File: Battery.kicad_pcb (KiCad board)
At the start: 2 copper layers, 95.9 x 90.2 mm, 10 parts, among them J1 PC104-8BIT, J2 PC104PTH, J3 PC104PTH, J4 PC104PTH, J5 PC104PTH

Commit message: balancing enabled by default using 1k PD. Can override by pulling line high from OBC
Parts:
- turned BT2 to 270 degrees
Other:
- board text removed: "GPS Coax slot location and dimentions are provisional. Consider structural integrity of the board with cables connected."
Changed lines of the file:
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@@
 (kicad_pcb (version 4) (host pcbnew 4.0.7-e2-6376~58~ubuntu16.04.1)
   (general
-    (links 0)
+    (links 1)
     (no_connects 1)
-    (area 104.924999 44.754999 200.965001 135.075001)
+    (area 20.5 22.899999 253.885715 168.15)
     (thickness 1.6)
-    (drawings 25)
+    (drawings 24)
     (tracks 0)
     (zones 0)
@@
   )
   (module SFUSat:1042-BattHolder (layer F.Cu)
-    (at 169 90 90)
-    (fp_text reference BT2 (at -40.2 7.6 360) (layer F.SilkS)
-      (effects (font (size 1 1) (thickness 0.15)))
-    )
-    (fp_text value Battery_Cell (at 11.8 -11.8 90) (layer F.Fab)
+    (at 169 90 270)
+    (fp_text reference BT2 (at -40.2 7.6 540) (layer F.SilkS)
+      (effects (font (size 1 1) (thickness 0.15)))
+    )
+    (fp_text value Battery_Cell (at 11.8 -11.8 270) (layer F.Fab)
       (effects (font (size 1 1) (thickness 0.15)))
     )
@@
     (fp_line (start -38.6 -10.4) (end 38.45 -10.4) (layer F.SilkS) (width 0.15))
     (fp_line (start -38.6 10.25) (end 38.45 10.25) (layer F.SilkS) (width 0.15))
-    (pad "" np_thru_hole circle (at 27.6 -8 90) (size 4.5 4.5) (drill 3.45) (layers *.Cu *.Mask))
-    (pad "" np_thru_hole circle (at -27.6 8 90) (size 4.5 4.5) (drill 3.45) (layers *.Cu *.Mask))
-    (pad "" np_thru_hole circle (at 35.82 8 90) (size 3.3 3.3) (drill 2.39) (layers *.Cu *.Mask))
-    (pad 2 smd rect (at 39.67 0 90) (size 7.46 6.47) (layers F.Cu F.Paste F.Mask)
+    (pad "" np_thru_hole circle (at 27.6 -8 270) (size 4.5 4.5) (drill 3.45) (layers *.Cu *.Mask))
+    (pad "" np_thru_hole circle (at -27.6 8 270) (size 4.5 4.5) (drill 3.45) (layers *.Cu *.Mask))
+    (pad "" np_thru_hole circle (at 35.82 8 270) (size 3.3 3.3) (drill 2.39) (layers *.Cu *.Mask))
+    (pad 2 smd rect (at 39.67 0 270) (size 7.46 6.47) (layers F.Cu F.Paste F.Mask)
       (net 70 GND))
-    (pad 1 smd rect (at -39.67 0 90) (size 7.46 6.47) (layers F.Cu F.Paste F.Mask)
+    (pad 1 smd rect (at -39.67 0 270) (size 7.46 6.47) (layers F.Cu F.Paste F.Mask)
       (net 68 "Net-(BT1-Pad2)"))
     (model ../../../../../home/tobi/Cubesat/Battery/KiCad-Lib/SFUSat.pretty/1042.wrl
@@
     (effects (font (size 3 3) (thickness 0.3)))
   )
-  (gr_text "GPS Coax slot location and dimentions are provisional.\nConsider structural integrity of the board with cables connected." (at 20.5 65.5) (layer Cmts.User)
-    (effects (font (size 1.5 1.5) (thickness 0.3)) (justify left))
-  )
   (gr_line (start 105 44.83) (end 200.885 44.83) (layer Edge.Cuts) (width 0.15))

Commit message: layout complete
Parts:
- added C1: 0.1uF, SFUSat-cap:C_0603, F.Cu at (118.0, 69.2)
- added C2: 0.1uF, SFUSat-cap:C_0603, F.Cu at (114.8, 69.2)
- added C3: 0.33uF, SFUSat-cap:C_0805, F.Cu at (113.5, 72.5)
- added C4: 0.1uF, SFUSat-cap:C_0603, F.Cu at (115.8, 75.8)
- added G***: LOGO, SFUSat:SFUSat_15mm_2, B.Cu at (120.0, 72.0)
- added J10: TEST_1P, SFUSat:Measurement_Point_Round-SMD-Pad_Big, F.Cu at (109.0, 89.0)
- added J11: B3B-XH-A(LF)(SN), SFUSat:B3B-XH-A, B.Cu at (116.0, 96.0)
- added J12: B3B-XH-A(LF)(SN), SFUSat:B3B-XH-A, F.Cu at (116.0, 116.0)
- added J6: B3B-XH-A(LF)(SN), SFUSat:B3B-XH-A, F.Cu at (116.0, 106.0)
- added J7: TEST_1P, SFUSat:Measurement_Point_Round-SMD-Pad_Big, F.Cu at (108.0, 79.0)
- added J8: TEST_1P, SFUSat:Measurement_Point_Round-SMD-Pad_Big, F.Cu at (108.0, 75.0)
- added J9: TEST_1P, SFUSat:Measurement_Point_Round-SMD-Pad_Big, F.Cu at (115.0, 89.0)
- added R1: DNP, SFUSat-res:R_0402, F.Cu at (117.2, 77.5)
- added R2: 1k, SFUSat-res:R_0402, F.Cu at (115.2, 77.5)
- added R3: 160R, SFUSat-res:R_0603, F.Cu at (119.2, 72.8)
- added R4: 250R, SFUSat-res:R_0603, F.Cu at (117.2, 66.0)
- added R5: 100R, SFUSat-res:R_0603, F.Cu at (115.5, 66.0)
- added R6: 100R, SFUSat-res:R_0603, F.Cu at (118.5, 75.8)
- added R7: DNP, SFUSat-res:R_0603, F.Cu at (109.0, 83.0)
- added U1: BQ29209, SFUSat:VDFN-8, F.Cu at (116.2, 72.5)
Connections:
- BT2 pad 2: GND -> /SeriesBatteryCell/PACK-
- J1 pad 12A: Net-(J1-Pad12A) -> /OVR_VLT
- J1 pad 13A: Net-(J1-Pad13A) -> /~CB_EN
- J1 pad 1B: Net-(J1-Pad1B) -> GND
- J1 pad 32A: Net-(J1-Pad32A) -> GND
- J1 pad 32B: Net-(J1-Pad32B) -> GND
- J2 pad 1: Net-(J2-Pad1) -> GND
- J3 pad 1: Net-(J3-Pad1) -> GND
- J4 pad 1: Net-(J4-Pad1) -> GND
- J5 pad 1: Net-(J5-Pad1) -> GND
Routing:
- net /SeriesBatteryCell/PACK-: track 0.00 -> 142.0 mm, vias 0 -> 10
- net /OVR_VLT: track 0.00 -> 98.5 mm, vias 0 -> 2
- net /~CB_EN: track 0.00 -> 98.2 mm, vias 0 -> 2
- net /SeriesBatteryCell/PACK+: track 0.00 -> 90.0 mm
- net Net-(BT1-Pad2): track 0.00 -> 66.1 mm
- net Net-(J11-Pad1): track 0.00 -> 20.0 mm
- net Net-(C1-Pad2): track 0.00 -> 6.04 mm
- net Net-(C1-Pad1): track 0.00 -> 4.84 mm
- net Net-(R5-Pad2): track 0.00 -> 4.45 mm, vias 0 -> 2
- net Net-(C4-Pad1): track 0.00 -> 3.06 mm
- net Net-(C3-Pad1): track 0.00 -> 1.97 mm
- net GND: track 0.00 -> 1.25 mm, vias 0 -> 1
- added copper zone on F.Cu, net /SeriesBatteryCell/PACK-
- added copper zone on B.Cu, net GND
- added copper zone on F.Cu, net GND
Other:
- board text added: "COM"
- board text added: "DEPLOYMENT"
- board text added: "EN"
- board text added: "NC"
- board text added: "OV"
- board text added: "SFU Satellite Design Team Battery Board Rev. 1"
- board text added: "over voltage"
- board text added: "pack+"
- board text added: "pack-"
- board text added: "return"

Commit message: moved bottom side DC connector to avoid the RFB pin path on the eps board
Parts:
- moved J11 7.21 mm to (112.0, 90.0)
- moved J10 4.21 mm to (110.3, 85.0)
- moved J9 4.12 mm to (116.0, 85.0)
- moved R7 1.02 mm to (108.8, 82.0)
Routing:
- net /SeriesBatteryCell/PACK+: track 90.0 -> 79.9 mm
- net Net-(J11-Pad1): track 20.0 -> 27.7 mm
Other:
- board text added: "+"
- board text added: "-"
- board text added: "1A"
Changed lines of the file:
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@@
     (links 43)
     (no_connects 0)
-    (area 104.924999 44.754999 200.965001 135.075001)
+    (area 83.114286 22.899999 253.885715 168.15)
     (thickness 1.6)
-    (drawings 40)
-    (tracks 134)
+    (drawings 45)
+    (tracks 136)
     (zones 0)
     (modules 30)
@@
   (module SFUSat:1042-BattHolder (layer F.Cu)
     (at 169 90 270)
-    (fp_text reference BT2 (at -40.2 7.6 540) (layer F.SilkS)
+    (fp_text reference BT2 (at -40.6 -5.6 540) (layer F.SilkS)
       (effects (font (size 1 1) (thickness 0.15)))
     )
@@
   )
   (module SFUSat:Measurement_Point_Round-SMD-Pad_Big (layer F.Cu)
-    (at 115 89)
+    (at 116 85)
     (descr "Mesurement Point, Round, SMD Pad, DM 3mm,")
     (tags "Mesurement Point Round SMD Pad 3mm")
@@
   )
   (module SFUSat:Measurement_Point_Round-SMD-Pad_Big (layer F.Cu)
-    (at 109 89)
+    (at 110.3 85)
     (descr "Mesurement Point, Round, SMD Pad, DM 3mm,")
     (tags "Mesurement Point Round SMD Pad 3mm")
@@
   )
   (module SFUSat:B3B-XH-A (layer B.Cu)
-    (at 116 96)
-    (fp_text reference J11 (at -6 1 90) (layer B.SilkS)
+    (at 112 90)
+    (fp_text reference J11 (at -0.1 4.8 180) (layer B.SilkS)
       (effects (font (size 1 1) (thickness 0.15)) (justify mirror))
     )
@@
   )
   (module SFUSat-res:R_0603 (layer F.Cu)
-    (at 109 83 180)
+    (at 108.8 82 180)
     (descr "Resistor SMD 0603, reflow soldering, Vishay (see dcrcw.pdf)")
     (tags "resistor 0603")
     (attr smd)
-    (fp_text reference R7 (at 0 -1.45 180) (layer F.SilkS)
+    (fp_text reference R7 (at 2.5 0.1 180) (layer F.SilkS)
       (effects (font (size 1 1) (thickness 0.15)))
     )
@@
       (xy -0.05114 -0.609094)) (layer B.SilkS) (width 0.01))
   )
+  (gr_text 1A (at 190.8 131.9) (layer F.SilkS)
+    (effects (font (size 1.5 1.5) (thickness 0.3)))
+  )
+  (gr_text - (at 162.9 130.4) (layer F.SilkS)
+    (effects (font (size 3 3) (thickness 0.3)))
+  )
+  (gr_text + (at 162.8 48) (layer F.SilkS)
+    (effects (font (size 3 3) (thickness 0.3)))
+  )
+  (gr_text - (at 130.9 48.5) (layer F.SilkS)
+    (effects (font (size 3 3) (thickness 0.3)))
+  )
+  (gr_text + (at 130.3 130.9) (layer F.SilkS)
+    (effects (font (size 3 3) (thickness 0.3)))
+  )
+  (gr_text "SFU Satellite Design Team\nBattery Board Rev. 1" (at 112 73 270) (layer B.SilkS)
+    (effects (font (size 1.5 1.5) (thickness 0.2)) (justify mirror))
+  )
   (gr_text OV (at 194 101) (layer F.SilkS)
     (effects (font (size 1 1) (thickness 0.15)))
   )
-  (gr_text EN (at 194 98 360) (layer F.SilkS)
+  (gr_text EN (at 194 98) (layer F.SilkS)
     (effects (font (size 1 1) (thickness 0.15)))
-  )
-  (gr_text "SFU Satellite Design Team\nBattery Board Rev. 1" (at 112 73 270) (layer B.SilkS)
-    (effects (font (size 1.5 1.5) (thickness 0.2)) (justify mirror))
   )
   (gr_text DEPLOYMENT (at 108 116 270) (layer F.SilkS)
@@
     (effects (font (size 1 1) (thickness 0.15)))
   )
-  (gr_text pack- (at 107 86 270) (layer F.SilkS)
+  (gr_text pack- (at 107.9 86.3 270) (layer F.SilkS)
     (effects (font (size 1 1) (thickness 0.15)))
   )
-  (gr_text pack+ (at 113 86 270) (layer F.SilkS)
+  (gr_text pack+ (at 113.5 85.4 270) (layer F.SilkS)
     (effects (font (size 1 1) (thickness 0.15)))
   )
@@
   (segment (start 147.088001 49.829999) (end 137.500001 49.829999) (width 5) (layer F.Cu) (net 59))
   (segment (start 137.500001 49.829999) (end 137 50.33) (width 5) (layer F.Cu) (net 59))
-  (segment (start 117.549999 92.549999) (end 117.549999 89) (width 1.5) (layer F.Cu) (net 60))
-  (segment (start 117.549999 89) (end 117.549999 86.450001) (width 1.5) (layer F.Cu) (net 60))
-  (segment (start 115 89) (end 117.549999 89) (width 1.5) (layer F.Cu) (net 60))
+  (segment (start 114.5 90) (end 114.5 91.13137) (width 1.5) (layer F.Cu) (net 60))
+  (segment (start 114.5 91.13137) (end 118.5 95.13137) (width 1.5) (layer F.Cu) (net 60))
+  (segment (start 118.5 95.13137) (end 118.5 100) (width 1.5) (layer F.Cu) (net 60))
+  (segment (start 116 85) (end 116 88.5) (width 1.5) (layer F.Cu) (net 60))
+  (segment (start 116 88.5) (end 114.5 90) (width 1.5) (layer F.Cu) (net 60))
+  (segment (start 117.549999 79.450001) (end 117.549999 83.450001) (width 1.5) (layer F.Cu) (net 60))
+  (segment (start 117.549999 83.450001) (end 116 85) (width 1.5) (layer F.Cu) (net 60))
   (segment (start 119.25 75.75) (end 119.25 77.75) (width 0.5) (layer F.Cu) (net 60))
   (segment (start 119.25 77.75) (end 119 78) (width 0.5) (layer F.Cu) (net 60))
@@
   (segment (start 118.5 77.5) (end 119 78) (width 0.3) (layer F.Cu) (net 60))
   (segment (start 117.549999 79.450001) (end 119 78) (width 1.5) (layer F.Cu) (net 60))
-  (segment (start 117.549999 86.450001) (end 117.549999 79.450001) (width 1.5) (layer F.Cu) (net 60))
-  (segment (start 118.5 93.5) (end 117.549999 92.549999) (width 1.5) (layer F.Cu) (net 60))
-  (segment (start 118.5 96) (end 118.5 93.5) (width 1.5) (layer F.Cu) (net 60))
-  (segment (start 118.5 96) (end 118.5 106) (width 1.5) (layer B.Cu) (net 60))
   (segment (start 118.5 106) (end 118.5 100) (width 1.5) (layer F.Cu) (net 60))
-  (segment (start 118.5 100) (end 118.5 96) (width 1.5) (layer F.Cu) (net 60))
   (segment (start 121 100) (end 118.5 100) (width 1.5) (layer F.Cu) (net 60))
   (segment (start 127 119.175) (end 127 100) (width 5) (layer F.Cu) (net 60))
@@
   (segment (start 137 129.175) (end 127 119.175) (width 5) (layer F.Cu) (net 60))
   (segment (start 119.25 73.5) (end 119.25 75.75) (width 0.5) (layer F.Cu) (net 60))
-  (segment (start 108.25 83) (end 107 83) (width 0.3) (layer F.Cu) (net 61))
-  (via (at 107 83) (size 0.6) (drill 0.4) (layers F.Cu B.Cu) (net 61))
-  (segment (start 116 96) (end 116 106) (width 1.5) (layer F.Cu) (net 62))
+  (segment (start 108.05 82) (end 108.05 83.15) (width 0.25) (layer F.Cu) (net 61))
+  (segment (start 108.05 83.15) (end 108 83.2) (width 0.25) (layer F.Cu) (net 61))
+  (via (at 108 83.2) (size 0.6) (drill 0.4) (layers F.Cu B.Cu) (net 61))
+  (segment (start 112 90) (end 112 102) (width 1.5) (layer F.Cu) (net 62))
+  (segment (start 112 102) (end 116 106) (width 1.5) (layer F.Cu) (net 62))
+  (segment (start 112 89) (end 112 90) (width 1.5) (layer F.Cu) (net 62))
+  (segment (start 112 83) (end 112 83.3) (width 0.5) (layer F.Cu) (net 62))
+  (segment (start 112 83.3) (end 110.3 85) (width 0.5) (layer F.Cu) (net 62))
+  (segment (start 112 83) (end 112 82) (width 1.5) (layer F.Cu) (net 62))
+  (segment (start 112 82) (end 112 79) (width 1.5) (layer F.Cu) (net 62))
+  (segment (start 109.55 82) (end 112 82) (width 0.5) (layer F.Cu) (net 62))
   (segment (start 112 89) (end 112 83) (width 1.5) (layer F.Cu) (net 62))
-  (segment (start 112 83) (end 112 79) (width 1.5) (layer F.Cu) (net 62))
-  (segment (start 109.75 83) (end 112 83) (width 0.3) (layer F.Cu) (net 62))
-  (segment (start 112 90) (end 112 89) (width 1.5) (layer F.Cu) (net 62))
-  (segment (start 109 89) (end 112 89) (width 1.5) (layer F.Cu) (net 62))
   (segment (start 114.8 77.5) (end 114.3 77.5) (width 0.3) (layer F.Cu) (net 62))
   (segment (start 114.3 77.5) (end 114 77.2) (width 0.3) (layer F.Cu) (net 62))
@@
   (segment (start 114 77) (end 114 75) (width 1.5) (layer F.Cu) (net 62))
   (segment (start 112 79) (end 114 77) (width 1.5) (layer F.Cu) (net 62))
-  (segment (start 116 94) (end 112 90) (width 1.5) (layer F.Cu) (net 62))
-  (segment (start 116 96) (end 116 94) (width 1.5) (layer F.Cu) (net 62))
   (segment (start 118.5 116) (end 118.5 108.5) (width 1.5) (layer B.Cu) (net 62))
   (segment (start 118.5 108.5) (end 116 106) (width 1.5) (layer B.Cu) (net 62))
@@
   (segment (start 117.975 73.975) (end 118 74) (width 0.25) (layer F.Cu) (net 69))
   (via (at 118 74) (size 0.6) (drill 0.4) (layers F.Cu B.Cu) (net 69))
+  (segment (start 109.5 90) (end 109.5 102) (width 1.5) (layer F.Cu) (net 70))
+  (segment (start 109.5 102) (end 113.5 106) (width 1.5) (layer F.Cu) (net 70))
   (segment (start 113.5 106) (end 113.5 116) (width 1.5) (layer F.Cu) (net 70))
-  (segment (start 113.5 96) (end 113.5 106) (width 1.5) (layer F.Cu) (net 70))
   (zone (net 62) (net_name /SeriesBatteryCell/PACK-) (layer F.Cu) (hatch edge 0.508)
     (priority 1)

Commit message: generated gerbers
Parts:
- moved G*** 2.20 mm to (121.7, 70.6)
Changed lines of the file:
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@@
     (visible_elements 7FFFFFFF)
     (pcbplotparams
-      (layerselection 0x00030_80000001)
+      (layerselection 0x010f8_80000001)
       (usegerberextensions false)
       (excludeedgelayer true)
@@
       (psa4output false)
       (plotreference true)
-      (plotvalue true)
+      (plotvalue false)
       (plotinvisibletext false)
       (padsonsilk false)
@@
       (drillshape 0)
       (scaleselection 1)
-      (outputdirectory ""))
+      (outputdirectory fab/))
   )
   (net 0 "")
@@
   (module SFUSat:PC104-8bit (layer F.Cu)
     (at 189.46 89.28)
-    (fp_text reference J1 (at -0.254 -43.815) (layer F.SilkS)
+    (fp_text reference J1 (at 0.04 -41.98) (layer F.SilkS)
       (effects (font (size 1 1) (thickness 0.15)))
     )
@@
   (module SFUSat:B3B-XH-A (layer B.Cu)
     (at 112 90)
-    (fp_text reference J11 (at -0.1 4.8 180) (layer B.SilkS)
+    (fp_text reference J11 (at -3.3 -3.3 180) (layer B.SilkS)
       (effects (font (size 1 1) (thickness 0.15)) (justify mirror))
     )
@@
   )
   (module SFUSat:SFUSat_15mm_2 (layer B.Cu)
-    (at 120 72 90)
+    (at 121.7 70.6 90)
     (fp_text reference G*** (at 0 0 90) (layer B.SilkS) hide
       (effects (font (thickness 0.3)) (justify mirror))
@@
     (effects (font (size 3 3) (thickness 0.3)))
   )
-  (gr_text "SFU Satellite Design Team\nBattery Board Rev. 1" (at 112 73 270) (layer B.SilkS)
+  (gr_text "SFU Satellite Design Team\nBattery Board Rev. 1" (at 112.4 71.6 270) (layer B.SilkS)
     (effects (font (size 1.5 1.5) (thickness 0.2)) (justify mirror))
   )
@@
     (effects (font (size 1 1) (thickness 0.15)))
   )
-  (gr_text pack+ (at 122 101) (layer B.SilkS)
+  (gr_text pack+ (at 115.1 94.3) (layer B.SilkS)
     (effects (font (size 1 1) (thickness 0.15)) (justify mirror))
   )
-  (gr_text pack- (at 116 101) (layer B.SilkS)
+  (gr_text pack- (at 111.4 95.9) (layer B.SilkS)
     (effects (font (size 1 1) (thickness 0.15)) (justify mirror))
   )
-  (gr_text return (at 110 101) (layer B.SilkS)
+  (gr_text return (at 107.6 94.5) (layer B.SilkS)
     (effects (font (size 1 1) (thickness 0.15)) (justify mirror))
   )

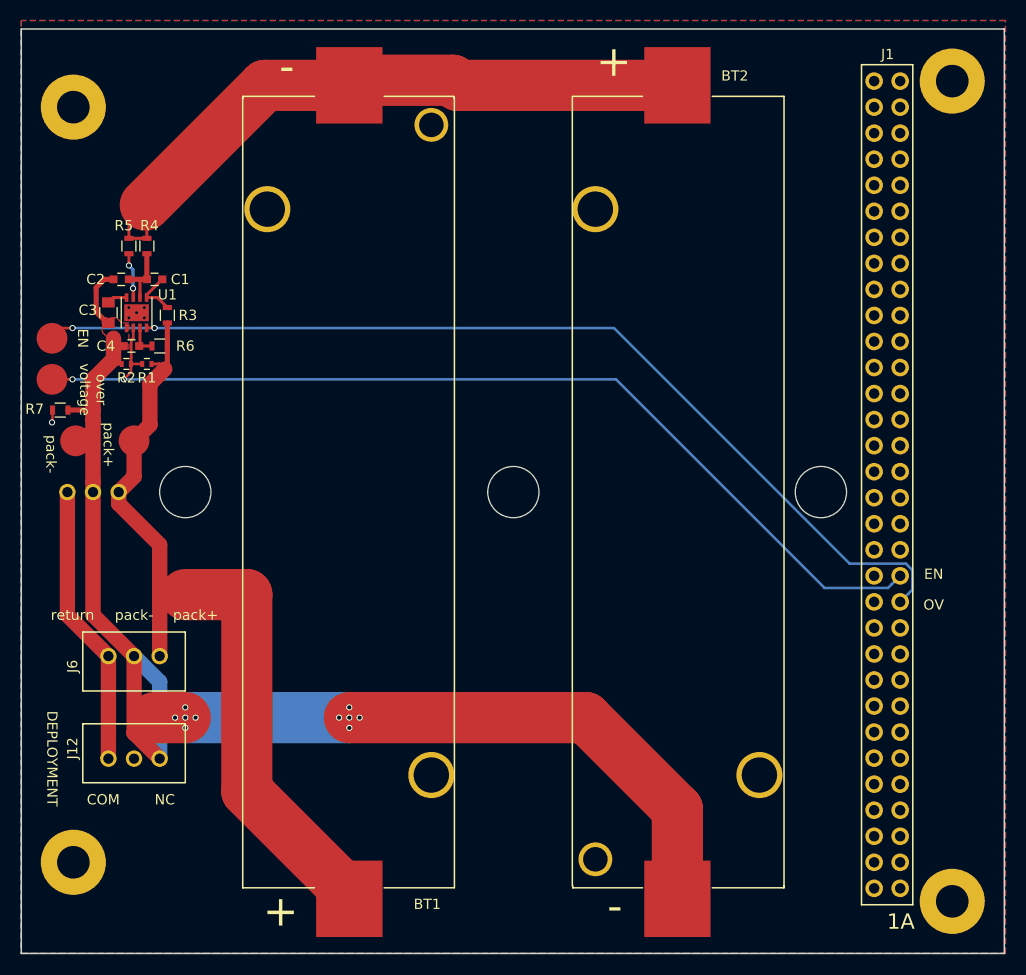
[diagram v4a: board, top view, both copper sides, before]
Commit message: Revision 2. Fixed silkscreen labelling issue with EN/OVR_VLT test points, Added level shifter for OVR_VLT output as IC outputs more than 3.3V
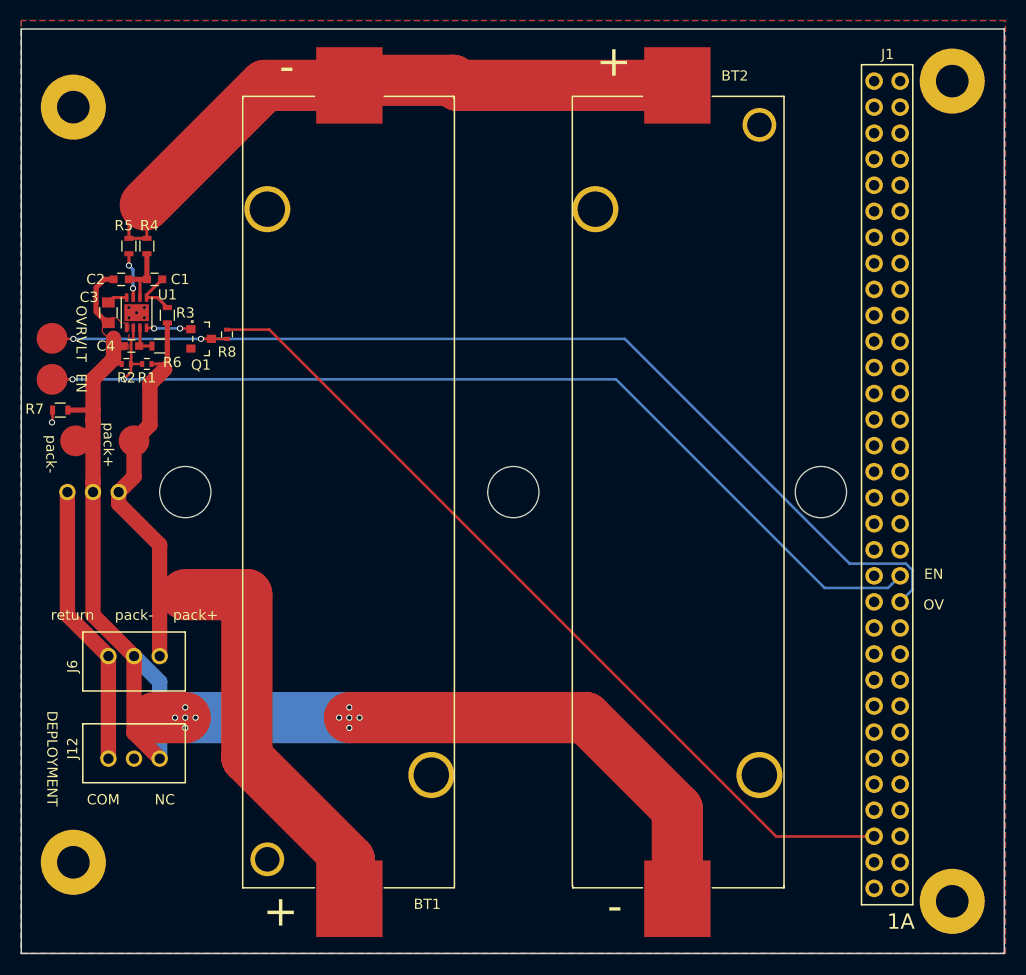
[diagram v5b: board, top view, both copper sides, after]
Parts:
- added Q1: 2N7002ET1G, SFUSat:SOT-23-3, F.Cu at (122.5, 75.1)
- added R8: R_10k0_1%_0.063W_0402, SFUSat-res:R_0402, F.Cu at (125.1, 74.6)
- BT2: footprint SFUSat:1042-BattHolder -> 1042-BattHolder
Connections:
- J1 pad 3B: Net-(J1-Pad3B) -> +3V3
- J1 pad 9B: (no net) -> Net-(J1-Pad9B)
- U1 pad 8: /OVR_VLT -> OUT
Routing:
- net +3V3: track 0.00 -> 83.6 mm
- net OUT: track 0.00 -> 4.37 mm, vias 0 -> 2
- net /OVR_VLT: track 98.5 -> 99.4 mm
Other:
- board text added: "OVRVLT"
- board text added: "SFU Satellite Design Team Battery Board Rev. 2"
- board text removed: "SFU Satellite Design Team Battery Board Rev. 1"
- board text removed: "over voltage"
